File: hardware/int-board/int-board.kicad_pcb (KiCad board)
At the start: 2 copper layers, 59 x 85 mm, 33 parts, among them J1 PTSM 0,5/4-HH-2,5-THR, J2 PTSM 0,5/4-HH-2,5-THR, J3 PTSM 0,5/4-HH-2,5-THR, J4 PTSM 0,5/4-HH-2,5-THR, J5 Pi 40-pin socket, J6 PTSM 0,5/5-HH-2,5-THR, J7 PTSM 0,5/4-HH-2,5-THR, J8 SP-C SP-E COM, J9 GPIO breakout, U1 LTV-847, U2 LTV-847, U3 LTV-847

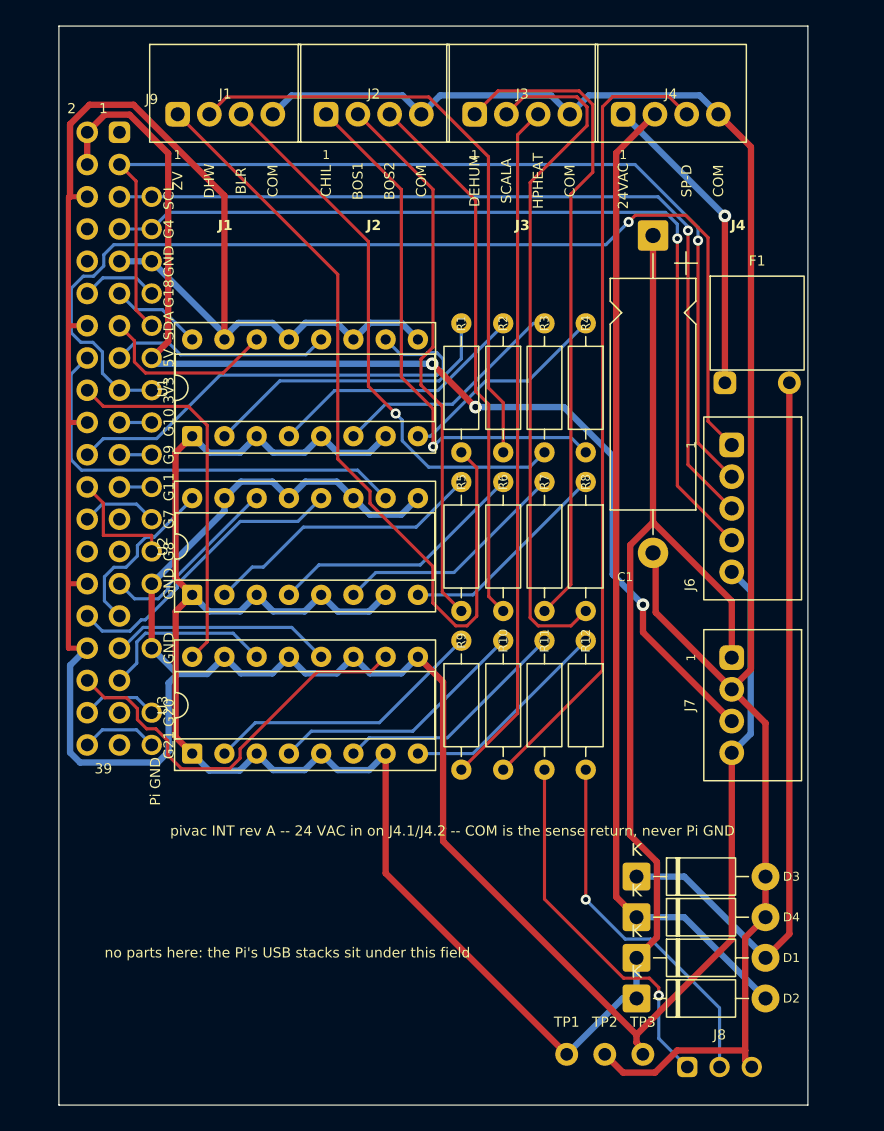
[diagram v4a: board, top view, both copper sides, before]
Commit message: hardware: link headers centred in the measured slot; pre-routed tracks locked for the router
The housing's right-hand slot measures y 26-59 from the board's top edge
(David, 2026-09-12), and two 4-way headers with their pins in the third
hole column from the edge fit it on the built board with a row between.
J6 and J7 move up to y 34.5 and 50.5, 1.4 mm from the slot's top and
2.65 mm from its bottom; the PTC moves up out of J6's way. That closes
the last physical check before the order.

Pre-routed tracks (the ground bus, GPIO8) are now locked, which KiCad
exports to Freerouting as fixed wiring: unlocked, the router sometimes
trimmed the bus and left a GND gap.

Co-Authored-By: Claude Fable 5.1 <noreply@anthropic.com>
Claude-Session: https://claude.ai/code/session_01WPMStupqhasFMcGr3goMno
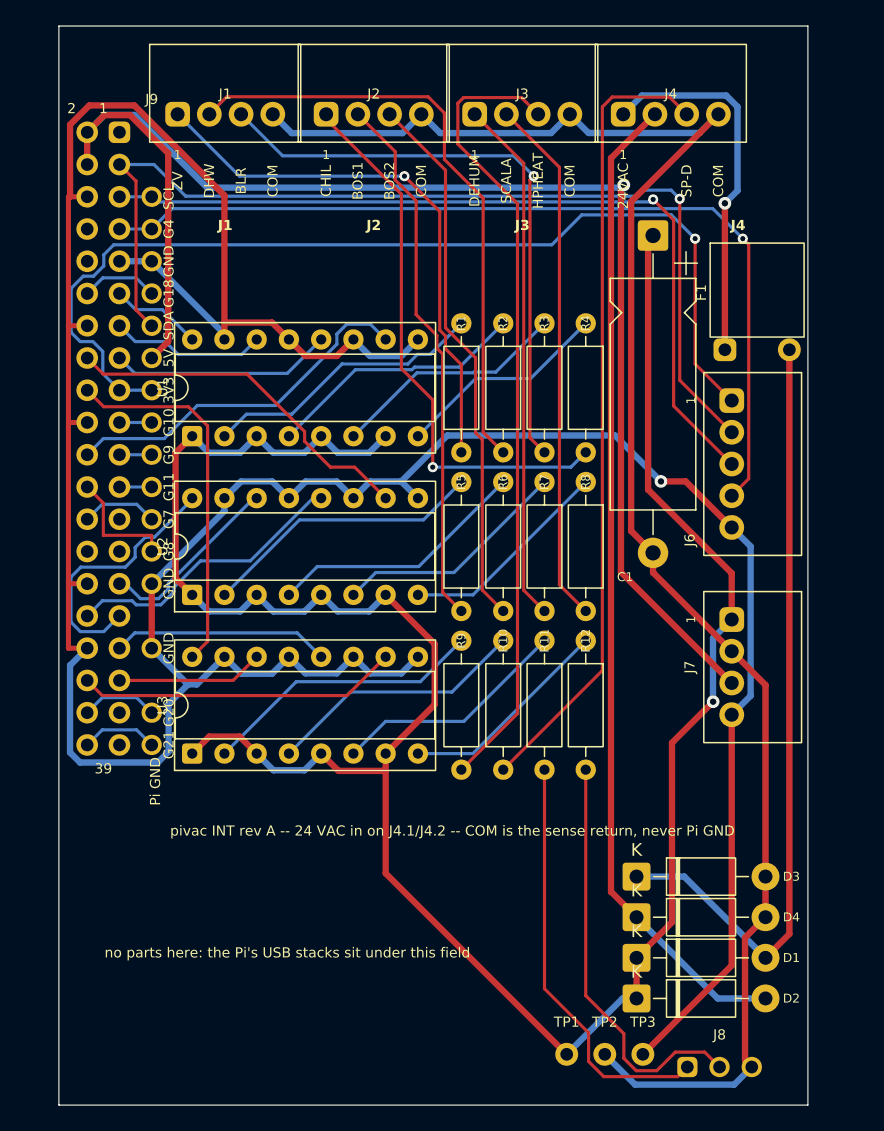
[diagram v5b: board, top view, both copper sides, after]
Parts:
- moved J6 3.50 mm to (53.0, 34.5)
- moved J7 3.00 mm to (53.0, 50.5)
- moved F1 2.60 mm to (55.0, 25.5)
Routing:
- net +5V: track 91.7 -> 115.6 mm, vias 3 -> 1
- net S_ZV: track 64.7 -> 43.5 mm, vias 0 -> 1
- net S_SCALA: track 54.5 -> 41.7 mm
- net S_DEHUM: track 52.0 -> 41.4 mm
- net S_HPHEAT: track 54.1 -> 63.3 mm
- net GPIO25: track 36.9 -> 28.7 mm
- net COM: track 143.1 -> 135.1 mm
- net VS: track 195.2 -> 187.3 mm, vias 0 -> 1
- net GPIO6: track 13.6 -> 20.8 mm
- net GPIO16: track 31.6 -> 25.3 mm
- net GPIO23: track 34.6 -> 28.5 mm
- net ACR: track 24.5 -> 29.5 mm
- net 3V3: track 83.6 -> 79.5 mm
- net S_SP-E: track 29.0 -> 33.0 mm, vias 1 -> 0
- net S_BLR: track 43.5 -> 47.4 mm
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
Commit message: hardware: F1's reference beside the J4 designator, clear of the capacitor
Co-Authored-By: Claude Fable 5.1 <noreply@anthropic.com>
Claude-Session: https://claude.ai/code/session_01WPMStupqhasFMcGr3goMno
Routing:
- net S_DHW: track 48.3 -> 36.2 mm
- net GPIO19: track 11.6 -> 21.7 mm
- net S_BLR: track 47.4 -> 37.6 mm
- net COM: track 135.1 -> 144.1 mm, vias 0 -> 1
- net GPIO6: track 20.8 -> 12.2 mm
- net S_CHIL: track 43.8 -> 36.1 mm
- net ACR: track 29.5 -> 21.9 mm, vias 1 -> 0
- net S_ZV: track 43.5 -> 36.7 mm, vias 1 -> 0
- net ACC: track 78.3 -> 83.5 mm
- net VS: track 187.3 -> 182.8 mm
- net S_HPHEAT: track 63.3 -> 58.9 mm, vias 0 -> 1
- net S_SP-C: track 33.0 -> 28.8 mm
- net S_SP-E: track 33.0 -> 29.0 mm
- net S_BOS1: track 42.5 -> 46.2 mm
- net +5V: track 115.6 -> 119.2 mm
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
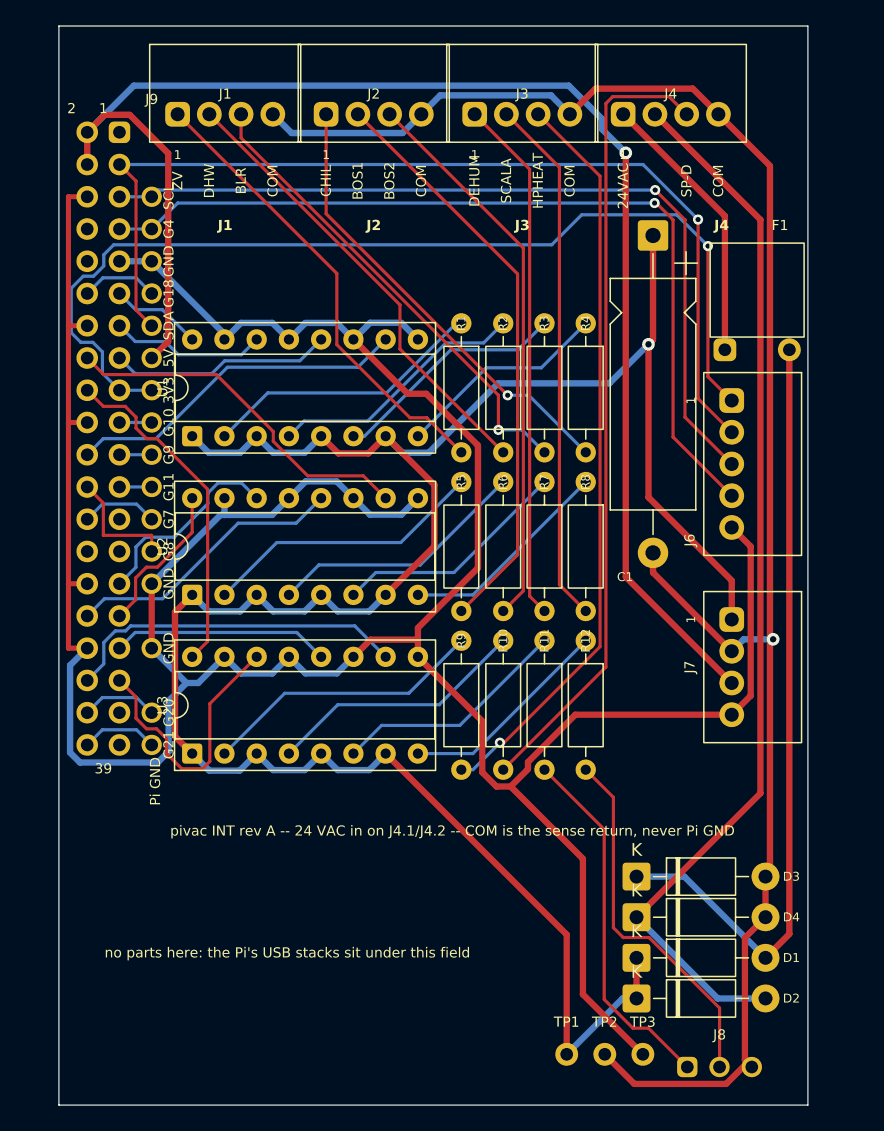
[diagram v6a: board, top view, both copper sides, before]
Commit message: Rev B boards generated: KiCad, schematics, BOMs and OSH Park gerbers for INT and EXT
gen-boards.py now builds rev B. INT loses the bridge, F1, C1, J7 and J8,
J4 carries HPCOOL, DHWX and SP-E, the sockets sit at x 13 with the resistor
columns on 4.0 mm (the most the housing bulges' rule areas allow), J6 is the
JST GH side-entry header at the slot with VS and COM on pins 6 and 7, and the
DL title block is centred in the bottom field. EXT keeps the probe sockets,
puts the I2C parts in one row under them, and carries the power section:
J3 24 VAC entry at the bottom edge with the sockets' 1.7 mm overhang, F1
standing, D1-D4 at 3.5 mm rows, C3 standing, U3 on a new SIP-8 footprint,
C4, J4 (XH) for the USB-C pigtail, a tie-slot pair, a 6 x 4 proto field and
the GH top-entry link header low at the opening, pin 1 at the bottom on both
boards. Freerouting is not deterministic, so build.sh regenerates and reroutes
each board until DRC is clean and everything is connected; five connections
it kept leaving open are laid as fixed tracks. Both boards are DRC-clean with
nothing unconnected; build.sh now also exports the gerbers and drill files
and zips them.

The plan carries the generated numbers and the state of the build; the layout
SVG matches it.

Co-Authored-By: Claude Fable 5.1 <noreply@anthropic.com>
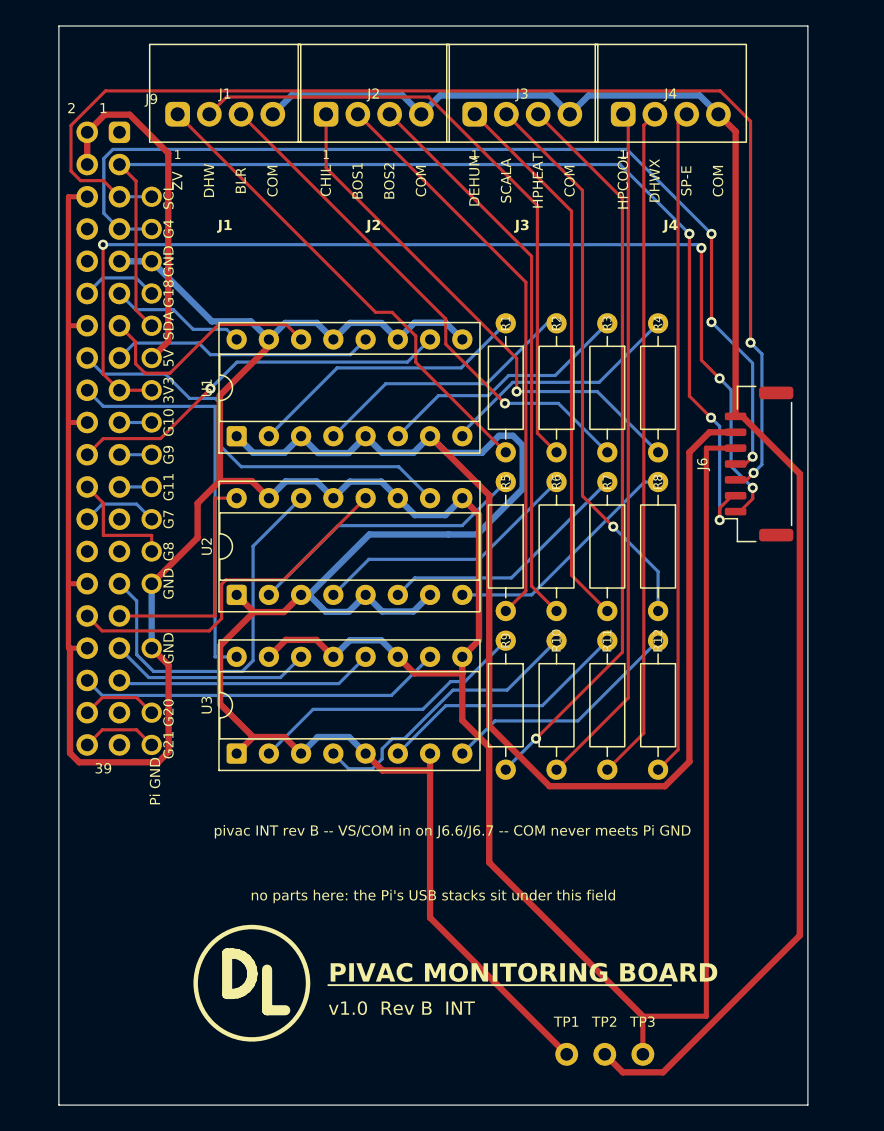
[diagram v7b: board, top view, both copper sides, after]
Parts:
- removed C1: 100u 63V axial, CP_Axial_L18.0mm_D6.5mm_P25.00mm_Horizontal
- removed D1, D2, D3, D4: 1N4007, D_DO-41_SOD81_P10.16mm_Horizontal
- removed F1: PTC 0.1A 60V, pivac:PTC_Radial_P5.08_Flat
- removed J7: PTSM 0,5/4-HH-2,5-THR, pivac:PTSM_0.5_4-HH-2.5-THR
- removed J8: SP-C SP-E COM, pivac:Pads_3x1
- J6: value PTSM 0,5/5-HH-2,5-THR -> GH SM07B link to EXT; footprint pivac:PTSM_0.5_5-HH-2.5-THR -> JST_GH_SM07B-GHS-TB_1x07-1MP_P1.25mm_Horizontal
- moved R12 5.70 mm to (47.2, 48.4)
- moved R4 5.70 mm to (47.2, 23.4)
- moved R8 5.70 mm to (47.2, 35.9)
- moved R11 4.95 mm to (43.2, 48.4)
- moved R3 4.95 mm to (43.2, 23.4)
- moved R7 4.95 mm to (43.2, 35.9)
- moved R10 4.20 mm to (39.2, 48.4)
- moved R2 4.20 mm to (39.2, 23.4)
- moved R6 4.20 mm to (39.2, 35.9)
- moved R1 3.50 mm to (35.2, 23.4)
- moved R5 3.50 mm to (35.2, 35.9)
- moved R9 3.50 mm to (35.2, 48.4)
- moved U1 3.50 mm to (14.0, 32.3)
- moved U2 3.50 mm to (14.0, 44.8)
- moved U3 3.50 mm to (14.0, 57.3)
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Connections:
- J4 pad 1: ACR -> S_HPCOOL
- J4 pad 2: ACC -> S_DHWX
- J4 pad 3: S_SP-D -> S_SP-E
- R10 pad 2: S_SP-D -> S_HPCOOL
- R11 pad 2: S_SP-C -> S_DHWX
- U3 pad 12: GPIO13 -> GPIO19
- U3 pad 14: GPIO19 -> GPIO13
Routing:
- net +5V: track 119.2 -> 27.4 mm, vias 1 -> 0
- net ACC: track 83.5 -> 0.00 mm
- net S_SP-D: track 63.0 -> 0.00 mm
- net ACF: track 61.5 -> 0.00 mm
- net S_HPCOOL: track 0.00 -> 54.1 mm
- net S_DHWX: track 0.00 -> 53.2 mm
- net SCL: track 66.5 -> 96.4 mm, vias 1 -> 2
- net S_SP-C: track 28.8 -> 0.00 mm
- net S_SP-E: track 29.0 -> 52.6 mm
- net ACR: track 21.9 -> 0.00 mm
- net COM: track 144.1 -> 126.9 mm, vias 1 -> 0
- net VS: track 182.8 -> 199.5 mm, vias 1 -> 0
- net GPIO5: track 16.0 -> 30.6 mm
- net S_DHW: track 36.2 -> 50.0 mm
- net GND: track 260.9 -> 273.1 mm
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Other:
- board text added: "DHWX"
- board text added: "HPCOOL"
- board text added: "LINK 3V3 SDA SCL G4 GND VS COM"
- board text added: "PIVAC MONITORING BOARD"
- board text added: "SP-E"
- board text added: "pivac INT rev B -- VS/COM in on J6.6/J6.7 -- COM never meets Pi GND"
- board text added: "v1.0 Rev B INT"
- board text removed: "24VAC"
- board text removed: "LINK 3V3 SDA SCL G4 GND"
- board text removed: "PWR VS COM 5V GND"
- board text removed: "SP-D"
- board text removed: "pivac INT rev A -- 24 VAC in on J4.1/J4.2 -- COM is the sense return, never Pi GND"

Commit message: INT: J6's pin legend on the front silkscreen beside the pads; the back-side legend served a through-hole header
Co-Authored-By: Claude Fable 5.1 <noreply@anthropic.com>
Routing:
- net 3V3: track 85.0 -> 123.9 mm, vias 4 -> 1
- net VS: track 199.5 -> 162.3 mm, vias 0 -> 1
- net SCL: track 96.4 -> 70.8 mm, vias 2 -> 1
- net GND: track 273.1 -> 296.3 mm, vias 0 -> 1
- net GPIO25: track 30.8 -> 45.3 mm, vias 1 -> 0
- net COM: track 126.9 -> 140.5 mm, vias 0 -> 1
- net GPIO4: track 80.0 -> 67.4 mm, vias 3 -> 1
- net S_CHIL: track 41.2 -> 52.5 mm, vias 1 -> 0
- net GPIO5: track 30.6 -> 20.6 mm, vias 0 -> 1
- net S_DHW: track 50.0 -> 40.5 mm, vias 0 -> 1
- net GPIO12: track 28.3 -> 36.8 mm
- net S_ZV: track 38.1 -> 44.2 mm
- net S_SCALA: track 44.1 -> 50.0 mm, vias 1 -> 0
- net S_HPHEAT: track 58.2 -> 63.1 mm
- net SDA: track 87.1 -> 90.5 mm, vias 3 -> 1
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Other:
- board text added: "J6 LINK 1=3V3 2=SDA 3=SCL 4=G4 5=GND 6=VS 7=COM"
- board text removed: "LINK 3V3 SDA SCL G4 GND VS COM"
